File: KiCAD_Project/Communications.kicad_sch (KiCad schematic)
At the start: 23 parts, among them J11 1-0000050, J12 1-0000190, U10 1-0000785, U11 1-0000464

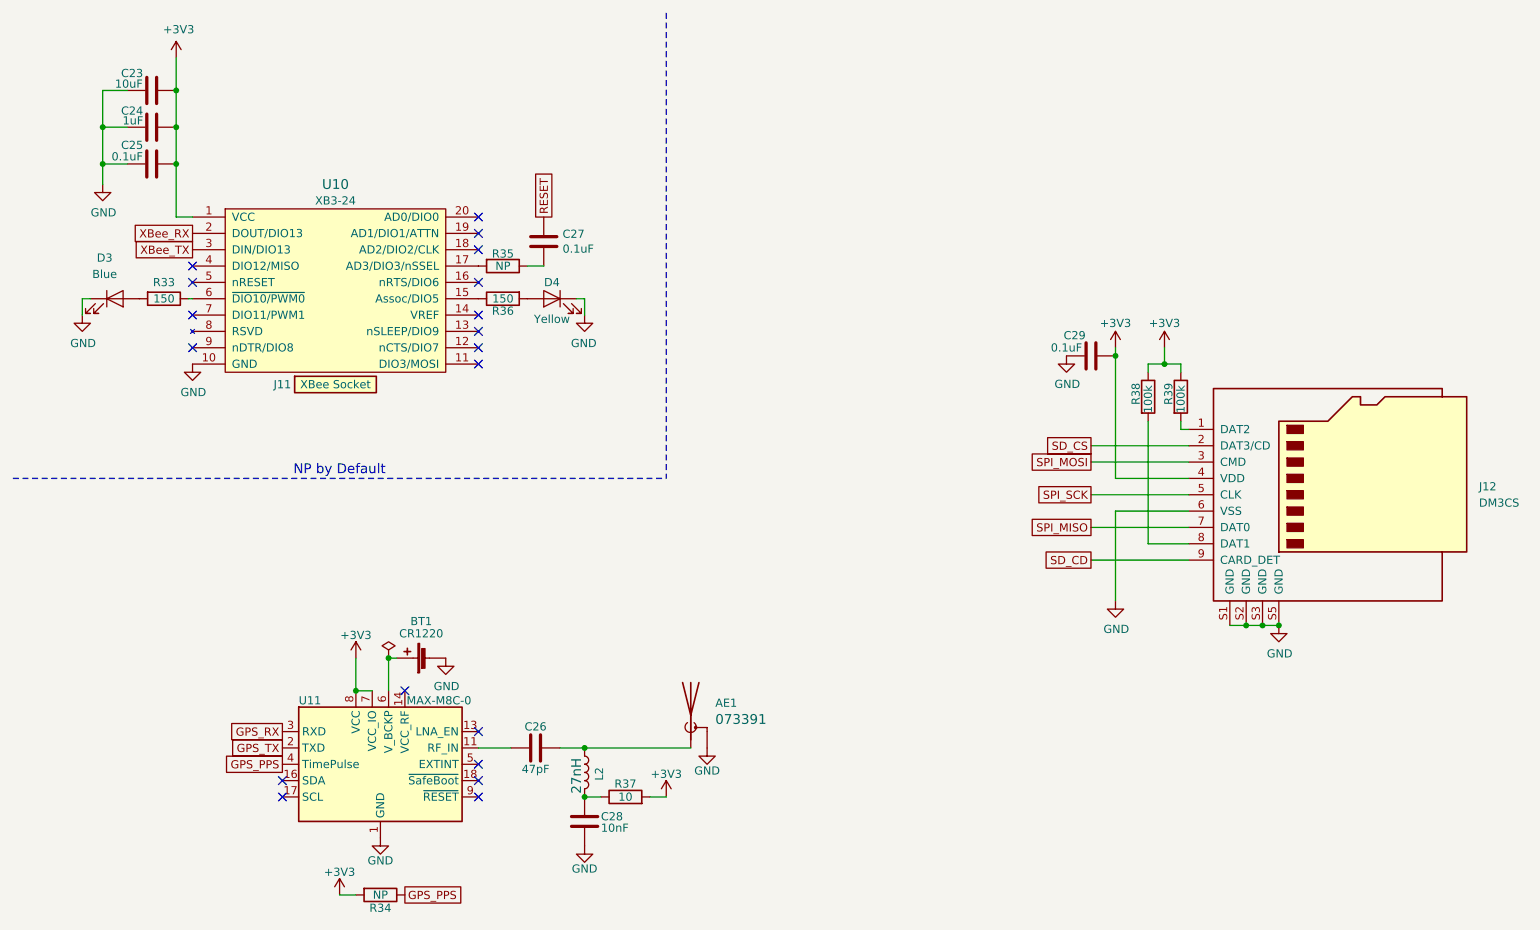
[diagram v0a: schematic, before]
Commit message: Rev 2.1 Changes: - Fixed Issue #11 (U4 Footprint pin 1 indicator) - Added Open Log Header for breakout - Removed SD Circuit - Connected GPS to I2C - Updated IPN and Revision Number
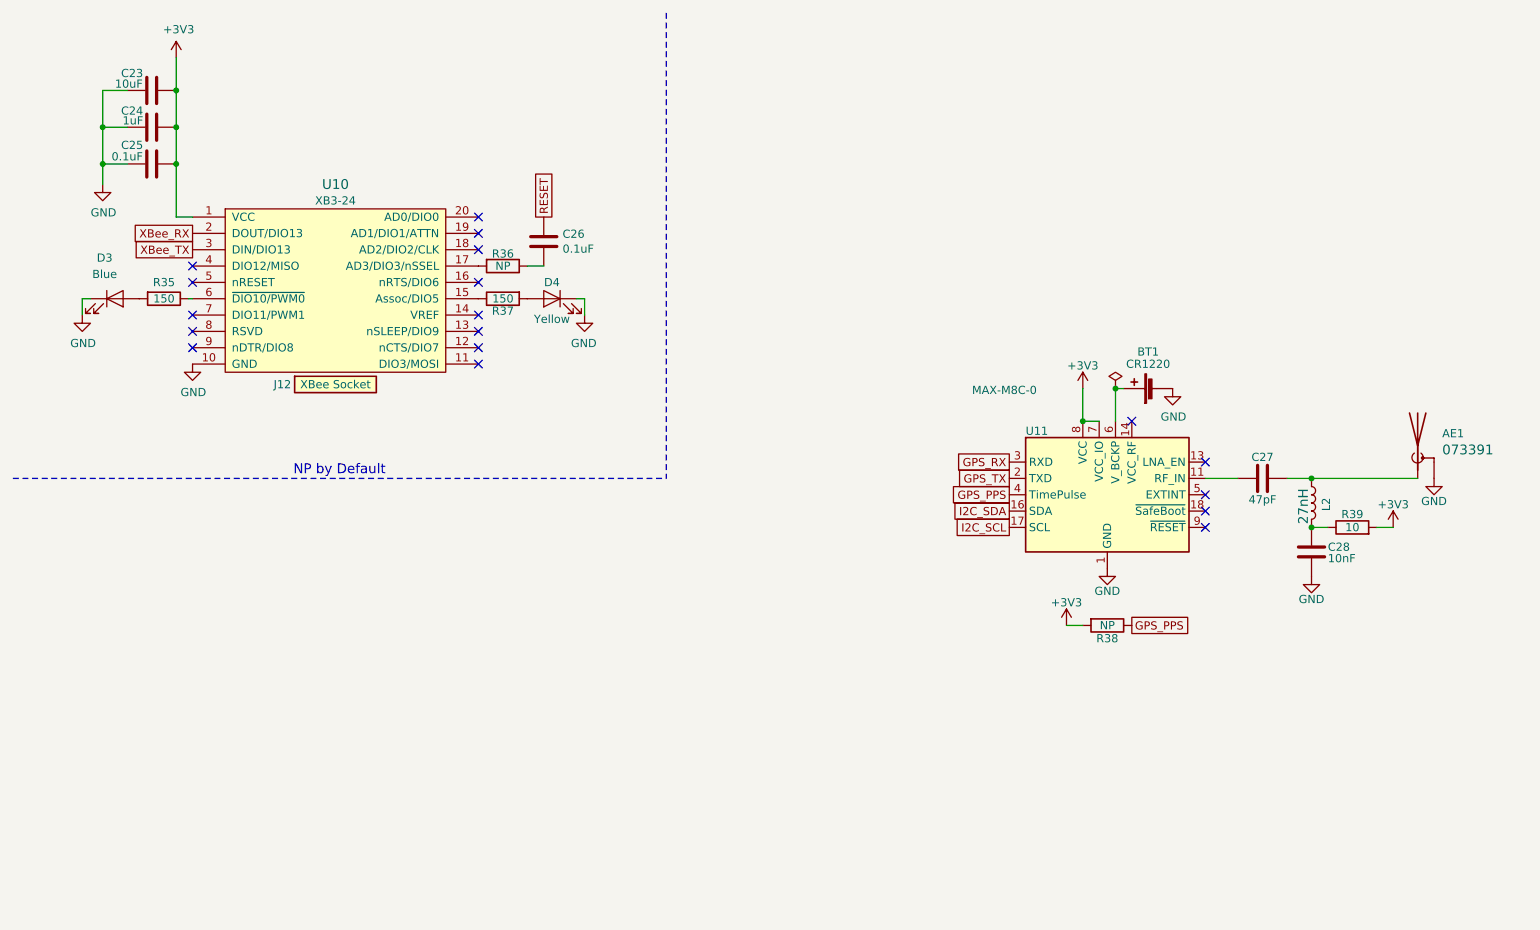
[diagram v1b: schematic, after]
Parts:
- removed C29: 1-0000007, capacitors_0603:1-0000007, symbol capacitors_0603:1-0000007
- removed J12: 1-0000190, connectors:1-0000190, symbol connectors:1-0000190
- removed R38, R39: 1-0000174, resistors_0603:1-0000174, symbol resistors_0603:1-0000174
- U10: Populated 0 -> 1
- renumbered C27 to C26, C26 to C27, J11 to J12, R33 to R35, R35 to R36, R36 to R37, R34 to R38, R37 to R39
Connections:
- net I2C_SDA: now reaches U11.16 (SDA)
- net I2C_SCL: now reaches U11.17 (SCL)
- no-connect marks 19 -> 18
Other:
- moved on the sheet: AE1, BT1, C27, C28, L2, R38, R39, U11
